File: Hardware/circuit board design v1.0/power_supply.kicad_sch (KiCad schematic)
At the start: 11 parts, among them J2 Conn_01x02, J3 105017-0001, U5 STF202-22T1G, U6 MAX40203_SOT23, U7 NCP161ASN180T1G

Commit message: Finished routing
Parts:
- J2: footprint Connector_JST:JST_PH_B2B-PH-K_1x02_P2.00mm_Vertical -> Components:JST_PH_B2B-PH-K_1x02_P2.00mm_Vertical
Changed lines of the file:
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@@
     (property "Reference" "J2" (id 0) (at 91.44 93.98 0))
     (property "Value" "Conn_01x02" (id 1) (at 91.44 96.52 0))
-    (property "Footprint" "Connector_JST:JST_PH_B2B-PH-K_1x02_P2.00mm_Vertical" (id 2) (at 91.44 102.87 0)
+    (property "Footprint" "Components:JST_PH_B2B-PH-K_1x02_P2.00mm_Vertical" (id 2) (at 91.44 102.87 0)
       (effects (font (size 1.27 1.27)) hide)
     )

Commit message: Changed connectors to horizontal
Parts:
- J2: footprint Components:JST_PH_B2B-PH-K_1x02_P2.00mm_Vertical -> Components:JST_PH_S2B-PH-K_1x02_P2.00mm_Horizontal
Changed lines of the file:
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@@
     (property "Reference" "J2" (id 0) (at 91.44 93.98 0))
     (property "Value" "Conn_01x02" (id 1) (at 91.44 96.52 0))
-    (property "Footprint" "Components:JST_PH_B2B-PH-K_1x02_P2.00mm_Vertical" (id 2) (at 91.44 102.87 0)
+    (property "Footprint" "Components:JST_PH_S2B-PH-K_1x02_P2.00mm_Horizontal" (id 2) (at 91.44 102.87 0)
       (effects (font (size 1.27 1.27)) hide)
     )

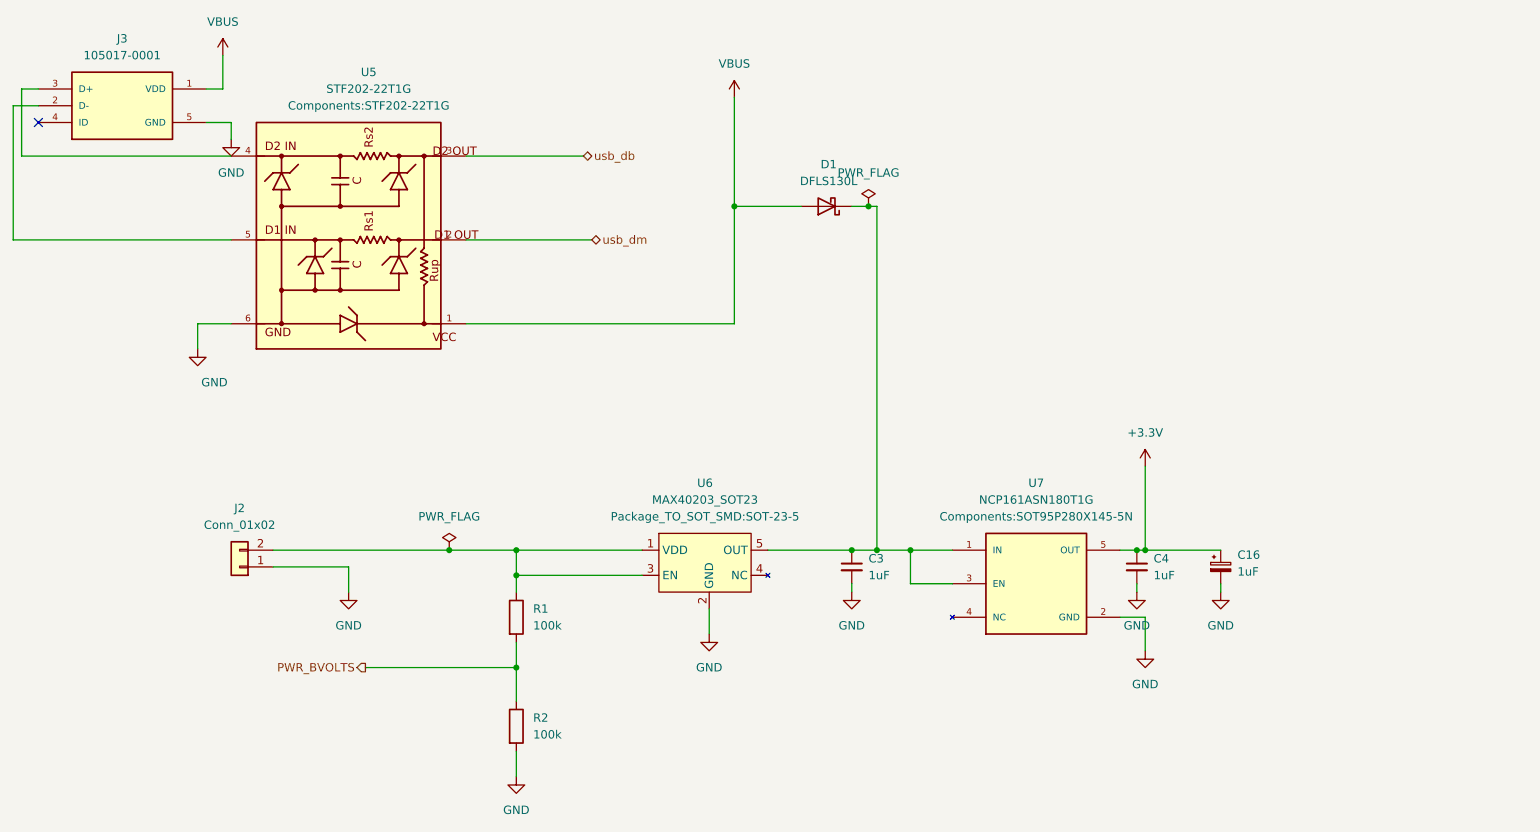
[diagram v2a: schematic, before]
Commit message: Added extra cap in case its needed
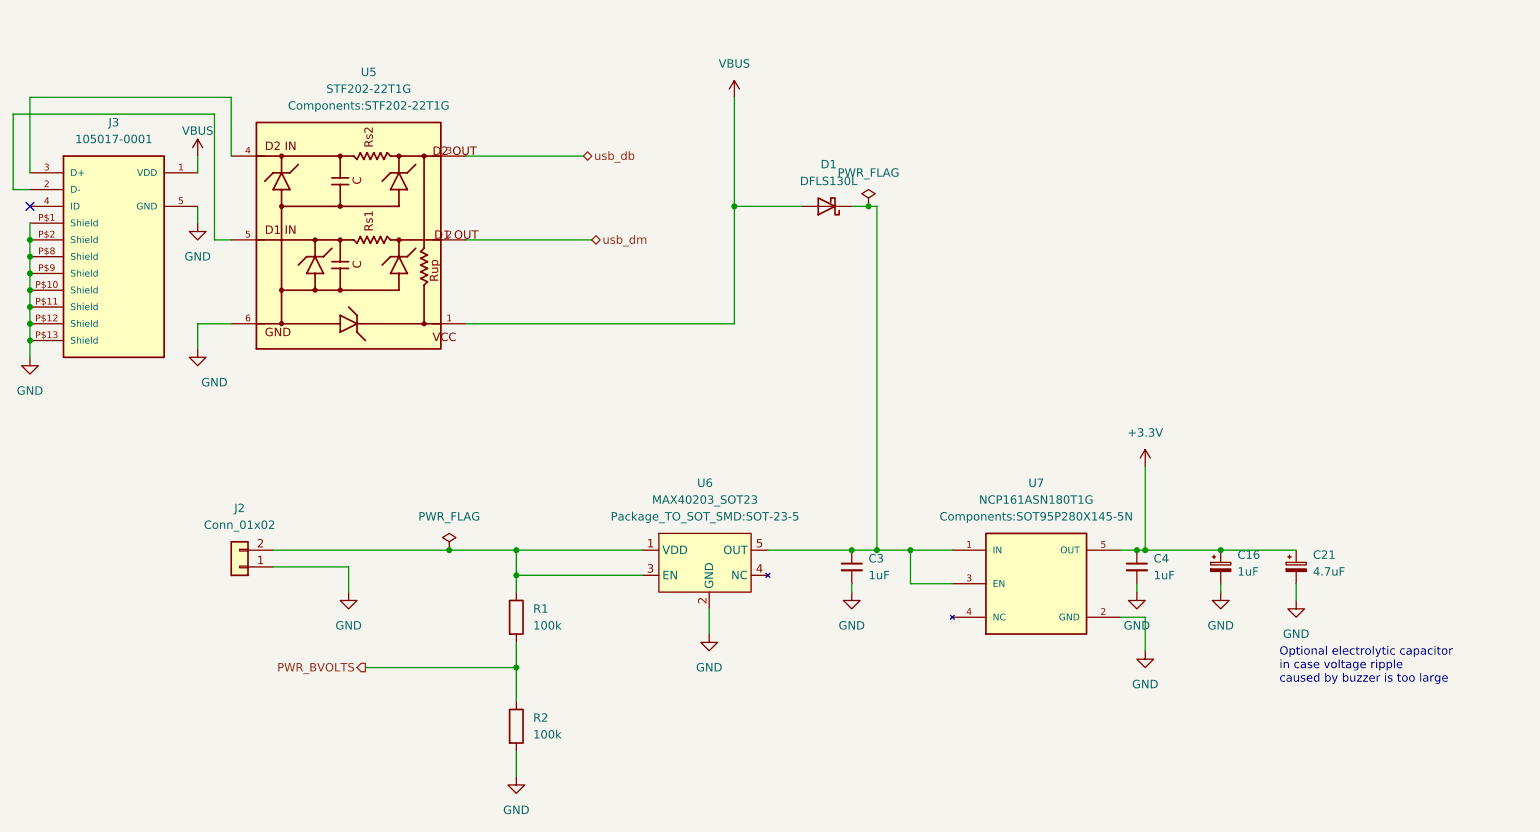
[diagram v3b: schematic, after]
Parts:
- added C21: 4.7uF, Capacitor_THT:CP_Radial_D5.0mm_P2.00mm, symbol Device:C_Polarized_Small
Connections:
- net +3.3V: now also C21.1
- net GND: now also J3.P$1 (Shield), J3.P$10 (Shield), J3.P$11 (Shield), J3.P$12 (Shield), J3.P$13 (Shield), J3.P$2 (Shield), J3.P$8 (Shield), J3.P$9 (Shield), C21.2
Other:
- note added: "Optional electrolytic capacitor in case voltage ripple caused by buzzer is too large"

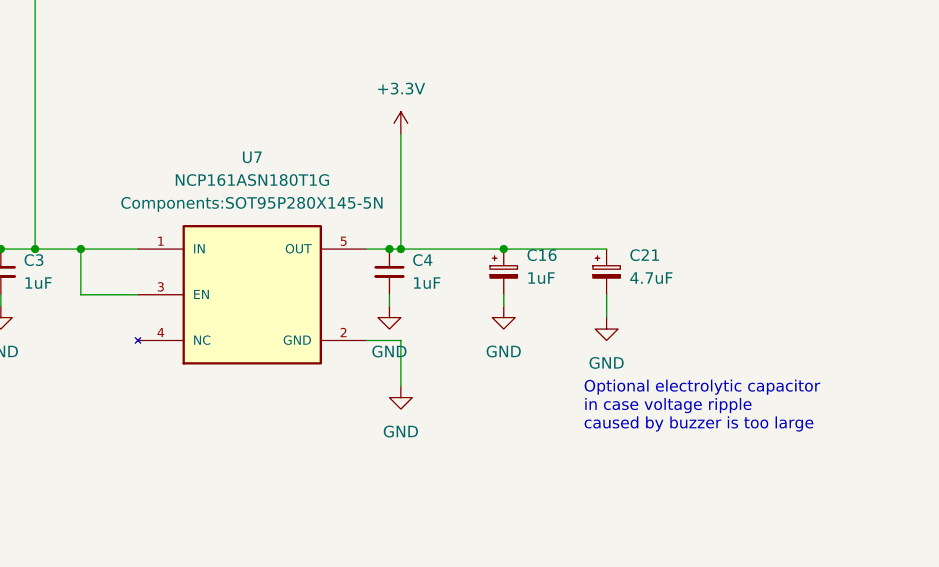
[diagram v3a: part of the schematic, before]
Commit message: Redid footprint for buzzer
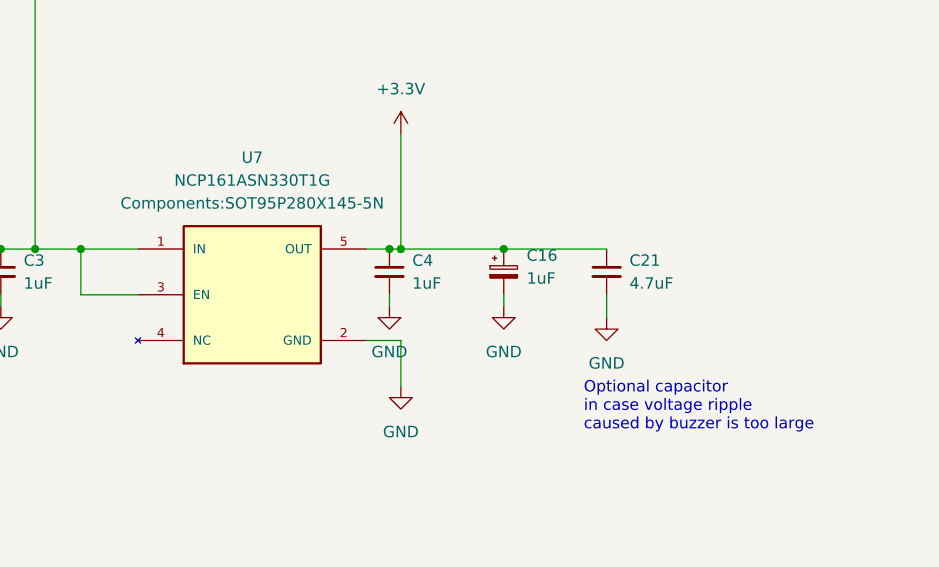
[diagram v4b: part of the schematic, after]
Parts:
- removed C21: 4.7uF, Capacitor_THT:CP_Radial_D5.0mm_P2.00mm, symbol Device:C_Polarized_Small
- added C21: 4.7uF, Capacitor_SMD:C_0603_1608Metric, symbol Device:C_Small
- U7: value NCP161ASN180T1G -> NCP161ASN330T1G
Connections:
- net +3.3V: now also C21.1
- net GND: now also C21.2
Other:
- note added: "Optional capacitor in case voltage ripple caused by buzzer is too large"
- note removed: "Optional electrolytic capacitor in case voltage ripple caused by buzzer is too large"
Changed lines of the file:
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@@
     (stroke (width 0) (type default) (color 0 0 0 0))
   )
-  (text "Optional electrolytic capacitor\nin case voltage ripple\ncaused by buzzer is too large"
+  (text "Optional capacitor\nin case voltage ripple\ncaused by buzzer is too large"
     (at 248.92 120.65 0)
     (effects (font (size 1.27 1.27)) (justify left bottom))
@@
     (in_bom yes) (on_board yes) (fields_autoplaced)
     (property "Reference" "U7" (id 0) (at 212.09 90.17 0))
-    (property "Value" "NCP161ASN180T1G" (id 1) (at 212.09 92.71 0))
+    (property "Value" "NCP161ASN330T1G" (id 1) (at 212.09 92.71 0))
     (property "Footprint" "Components:SOT95P280X145-5N" (id 2) (at 212.09 95.25 0))
-    (property "Datasheet" "" (id 3) (at 212.09 105.41 0)
+    (property "Datasheet" "https://www.mouser.co.uk/datasheet/2/308/1/NCP161_D-2316989.pdf" (id 3) (at 212.09 105.41 0)
       (effects (font (size 1.27 1.27)) hide)
     )
@@
     (pin "5")
   )
-  (symbol (lib_id "Device:C_Polarized_Small") (at 251.46 102.87 0) (unit 1)
-    (in_bom yes) (on_board yes) (fields_autoplaced)
-    (property "Reference" "C21" (id 0) (at 254 101.0538 0)
-      (effects (font (size 1.27 1.27)) (justify left))
-    )
-    (property "Value" "4.7uF" (id 1) (at 254 103.5938 0)
-      (effects (font (size 1.27 1.27)) (justify left))
-    )
-    (property "Footprint" "Capacitor_THT:CP_Radial_D5.0mm_P2.00mm" (id 2) (at 251.46 102.87 0)
-      (effects (font (size 1.27 1.27)) hide)
-    )
-    (property "Datasheet" "~" (id 3) (at 251.46 102.87 0)
-      (effects (font (size 1.27 1.27)) hide)
-    )
-    (pin "1")
-    (pin "2")
-  )
   (symbol (lib_id "power:GND") (at 184.15 106.68 0) (unit 1)
     (in_bom yes) (on_board yes) (fields_autoplaced)
@@
     (pin "1")
   )
+  (symbol (lib_id "Device:C_Small") (at 251.46 102.87 0) (unit 1)
+    (in_bom yes) (on_board yes) (fields_autoplaced)
+    (property "Reference" "C21" (id 0) (at 254 101.6062 0)
+      (effects (font (size 1.27 1.27)) (justify left))
+    )
+    (property "Value" "4.7uF" (id 1) (at 254 104.1462 0)
+      (effects (font (size 1.27 1.27)) (justify left))
+    )
+    (property "Footprint" "Capacitor_SMD:C_0603_1608Metric" (id 2) (at 251.46 102.87 0)
+      (effects (font (size 1.27 1.27)) hide)
+    )
+    (property "Datasheet" "~" (id 3) (at 251.46 102.87 0)
+      (effects (font (size 1.27 1.27)) hide)
+    )
+    (pin "1")
+    (pin "2")
+  )
   (symbol (lib_id "Device:R") (at 133.35 127 0) (unit 1)

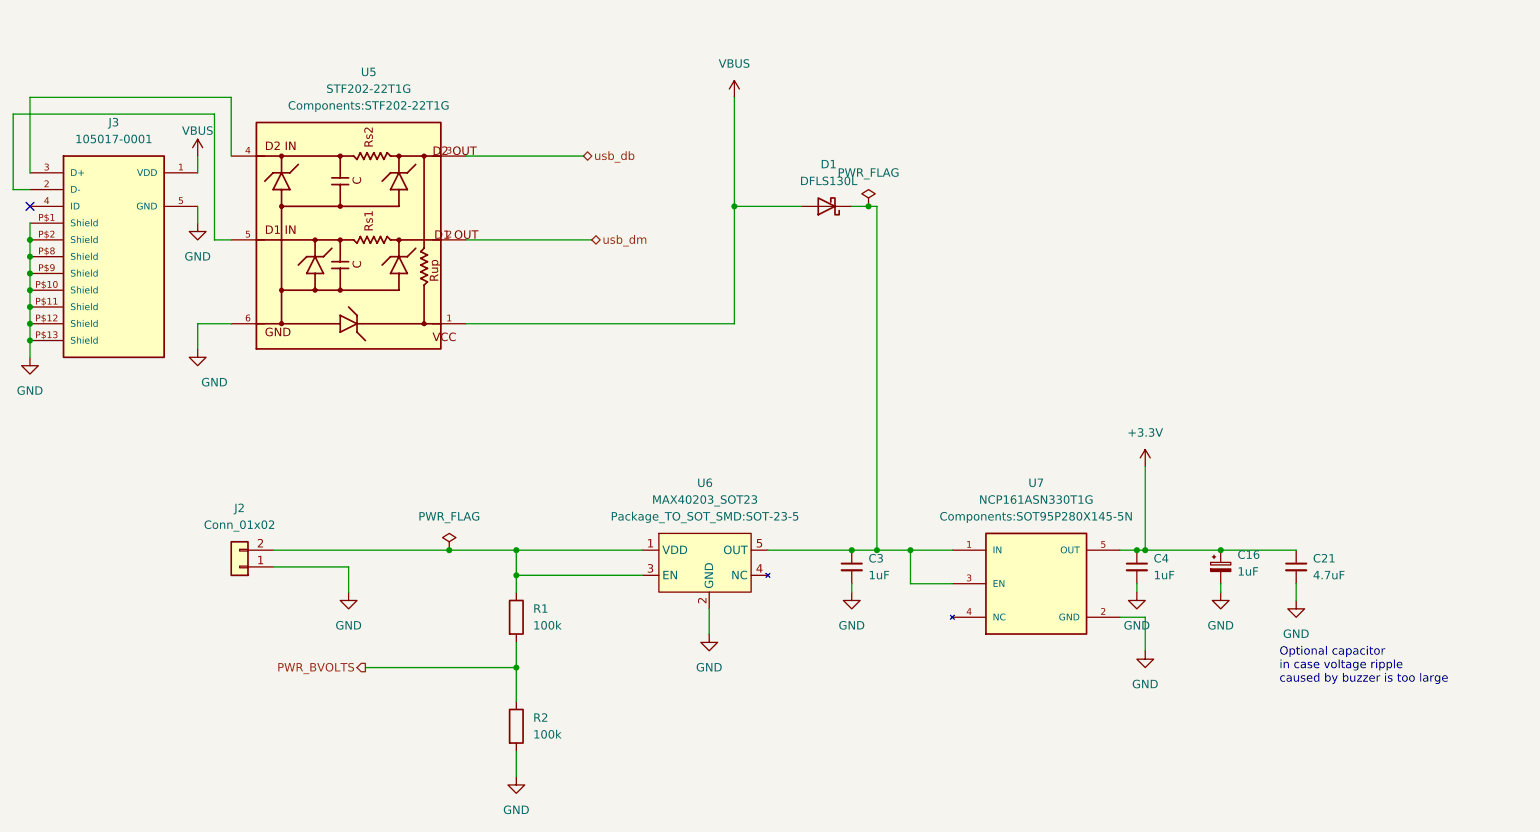
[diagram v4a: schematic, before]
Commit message: Added radio connections to pcb and code
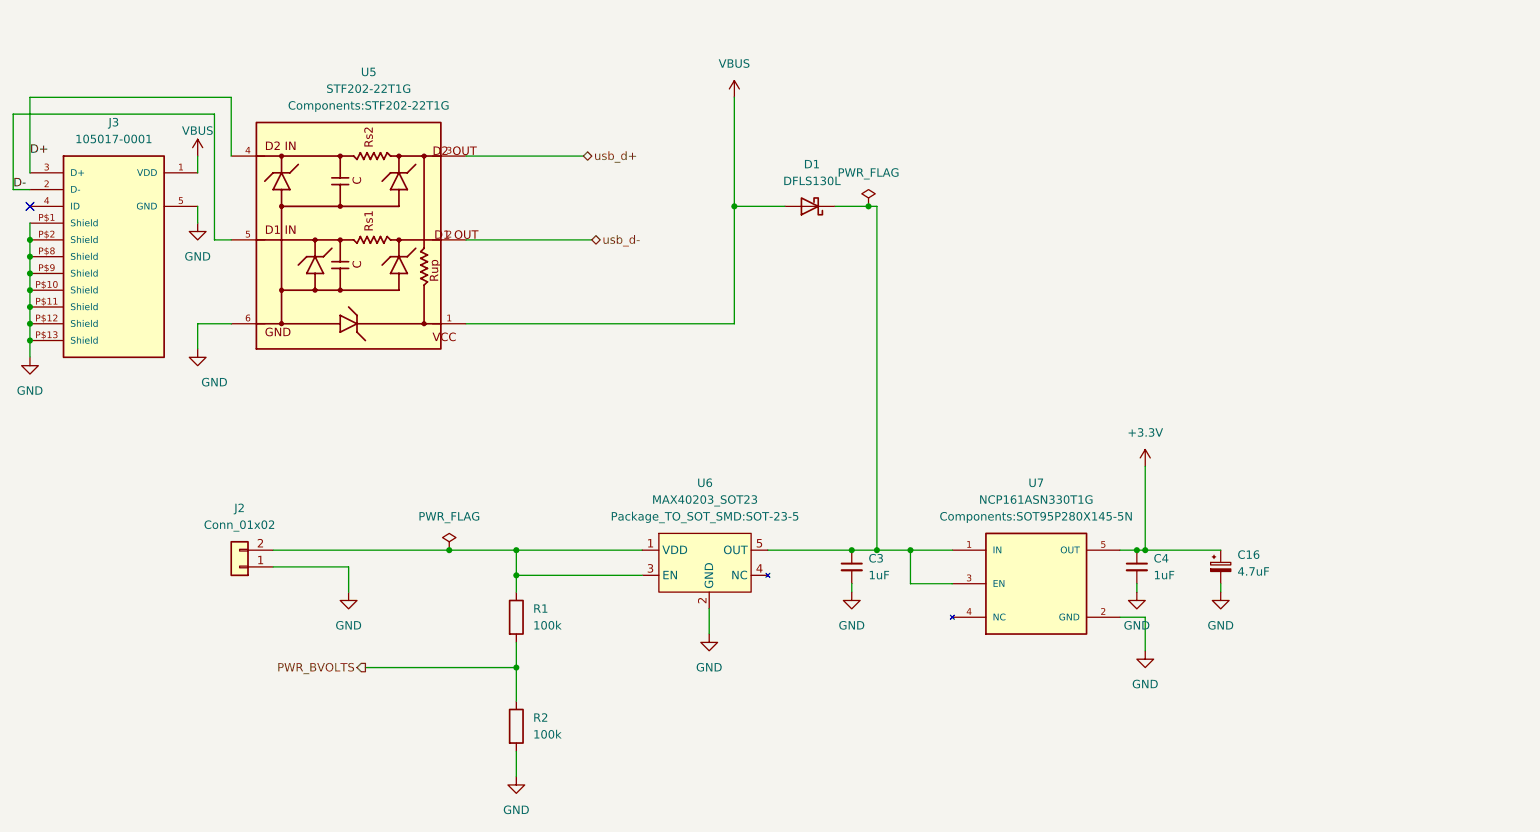
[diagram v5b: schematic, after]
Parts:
- removed C21: 4.7uF, Capacitor_SMD:C_0603_1608Metric, symbol Device:C_Small
- C16: value 1uF -> 4.7uF
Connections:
- net D-: now reaches J3.2 (D-), U5.5
- net D+: now reaches J3.3 (D+), U5.4
- net usb_db renamed usb_d+
- net usb_dm renamed usb_d-
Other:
- note removed: "Optional capacitor in case voltage ripple caused by buzzer is too large"
- moved on the sheet: D1
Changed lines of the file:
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@@
   (junction (at 184.15 100.33) (diameter 0) (color 0 0 0 0)
-  )
-  (junction (at 240.03 100.33) (diameter 0) (color 0 0 0 0)
   )
   (junction (at 186.69 48.26) (diameter 0) (color 0 0 0 0)
@@
     (stroke (width 0) (type default) (color 0 0 0 0))
   )
-  (wire (pts (xy 240.03 100.33) (xy 251.46 100.33))
-    (stroke (width 0) (type default) (color 0 0 0 0))
-  )
   (wire (pts (xy 87.63 53.34) (xy 90.17 53.34))
     (stroke (width 0) (type default) (color 0 0 0 0))
@@
     (stroke (width 0) (type default) (color 0 0 0 0))
   )
-  (wire (pts (xy 166.37 48.26) (xy 176.53 48.26))
+  (wire (pts (xy 166.37 48.26) (xy 173.99 48.26))
     (stroke (width 0) (type default) (color 0 0 0 0))
   )
@@
     (stroke (width 0) (type default) (color 0 0 0 0))
   )
-  (wire (pts (xy 184.15 48.26) (xy 186.69 48.26))
+  (wire (pts (xy 181.61 48.26) (xy 186.69 48.26))
     (stroke (width 0) (type default) (color 0 0 0 0))
   )
@@
     (stroke (width 0) (type default) (color 0 0 0 0))
   )
-  (wire (pts (xy 251.46 105.41) (xy 251.46 107.95))
-    (stroke (width 0) (type default) (color 0 0 0 0))
-  )
   (wire (pts (xy 59.69 31.75) (xy 59.69 43.18))
     (stroke (width 0) (type default) (color 0 0 0 0))
@@
     (stroke (width 0) (type default) (color 0 0 0 0))
   )
-  (text "Optional capacitor\nin case voltage ripple\ncaused by buzzer is too large"
-    (at 248.92 120.65 0)
+  (label "D+" (at 59.69 40.64 0)
     (effects (font (size 1.27 1.27)) (justify left bottom))
   )
-  (hierarchical_label "usb_dm" (shape bidirectional) (at 144.78 53.34 0)
+  (label "D-" (at 57.15 45.72 0)
+    (effects (font (size 1.27 1.27)) (justify left bottom))
+  )
+  (hierarchical_label "usb_d-" (shape bidirectional) (at 144.78 53.34 0)
     (effects (font (size 1.27 1.27)) (justify left))
   )
@@
     (effects (font (size 1.27 1.27)) (justify right))
   )
-  (hierarchical_label "usb_db" (shape bidirectional) (at 143.51 40.64 0)
+  (hierarchical_label "usb_d+" (shape bidirectional) (at 143.51 40.64 0)
     (effects (font (size 1.27 1.27)) (justify left))
   )
@@
       (effects (font (size 1.27 1.27)) (justify left))
     )
-    (property "Value" "1uF" (id 1) (at 242.57 103.5938 0)
+    (property "Value" "4.7uF" (id 1) (at 242.57 103.5938 0)
       (effects (font (size 1.27 1.27)) (justify left))
     )
@@
     )
     (pin "1")
-  )
-  (symbol (lib_id "Device:C_Small") (at 251.46 102.87 0) (unit 1)
-    (in_bom yes) (on_board yes) (fields_autoplaced)
-    (property "Reference" "C21" (id 0) (at 254 101.6062 0)
-      (effects (font (size 1.27 1.27)) (justify left))
-    )
-    (property "Value" "4.7uF" (id 1) (at 254 104.1462 0)
-      (effects (font (size 1.27 1.27)) (justify left))
-    )
-    (property "Footprint" "Capacitor_SMD:C_0603_1608Metric" (id 2) (at 251.46 102.87 0)
-      (effects (font (size 1.27 1.27)) hide)
-    )
-    (property "Datasheet" "~" (id 3) (at 251.46 102.87 0)
-      (effects (font (size 1.27 1.27)) hide)
-    )
-    (pin "1")
-    (pin "2")
   )
   (symbol (lib_id "Device:R") (at 133.35 127 0) (unit 1)
@@
     (pin "5")
   )
-  (symbol (lib_id "Components:DFLS130L") (at 180.34 48.26 180) (unit 1)
-    (in_bom yes) (on_board yes) (fields_autoplaced)
-    (property "Reference" "D1" (id 0) (at 180.6575 41.91 0))
-    (property "Value" "DFLS130L" (id 1) (at 180.6575 44.45 0))
-    (property "Footprint" "Components:PowerDI123" (id 2) (at 180.34 48.26 0)
-      (effects (font (size 1.27 1.27)) hide)
-    )
-    (property "Datasheet" "~" (id 3) (at 180.34 48.26 0)
+  (symbol (lib_id "Components:DFLS130L") (at 177.8 48.26 180) (unit 1)
+    (in_bom yes) (on_board yes) (fields_autoplaced)
+    (property "Reference" "D1" (id 0) (at 178.1175 41.91 0))
+    (property "Value" "DFLS130L" (id 1) (at 178.1175 44.45 0))
+    (property "Footprint" "Components:PowerDI123" (id 2) (at 177.8 48.26 0)
+      (effects (font (size 1.27 1.27)) hide)
+    )
+    (property "Datasheet" "~" (id 3) (at 177.8 48.26 0)
       (effects (font (size 1.27 1.27)) hide)
     )
@@
     (pin "2")
   )
-  (symbol (lib_name "GND_4") (lib_id "power:GND") (at 251.46 107.95 0) (unit 1)
-    (in_bom yes) (on_board yes) (fields_autoplaced)
-    (property "Reference" "#PWR0155" (id 0) (at 251.46 114.3 0)
-      (effects (font (size 1.27 1.27)) hide)
-    )
-    (property "Value" "GND" (id 1) (at 251.46 113.03 0))
-    (property "Footprint" "" (id 2) (at 251.46 107.95 0)
-      (effects (font (size 1.27 1.27)) hide)
-    )
-    (property "Datasheet" "" (id 3) (at 251.46 107.95 0)
-      (effects (font (size 1.27 1.27)) hide)
-    )
-    (pin "1")
-  )
   (symbol (lib_id "Device:C_Small") (at 184.15 102.87 0) (unit 1)
